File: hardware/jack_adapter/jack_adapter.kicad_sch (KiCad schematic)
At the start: 14 parts, among them J1 2.5mm Mic, J2 AudioPlug3, J3 3.5mm Headphones, J4 Header, SW1 SW_SPDT, SW2 SW_SPST

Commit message: feat: Moved the jacks slightly to be inline diagonally
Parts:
- J1: JLCPCB Part # C431535 -> C431536
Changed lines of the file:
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@@
 			)
 		)
-		(property "JLCPCB Part #" "C431535"
+		(property "JLCPCB Part #" "C431536"
 			(at 49.53 86.36 0)
 			(effects

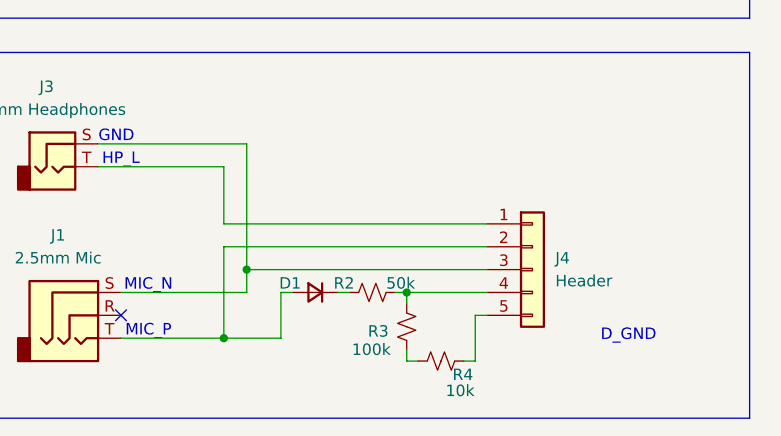
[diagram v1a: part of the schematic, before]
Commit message: feat: Changed resistor part number, and jumpers, and re-arranged things a bit
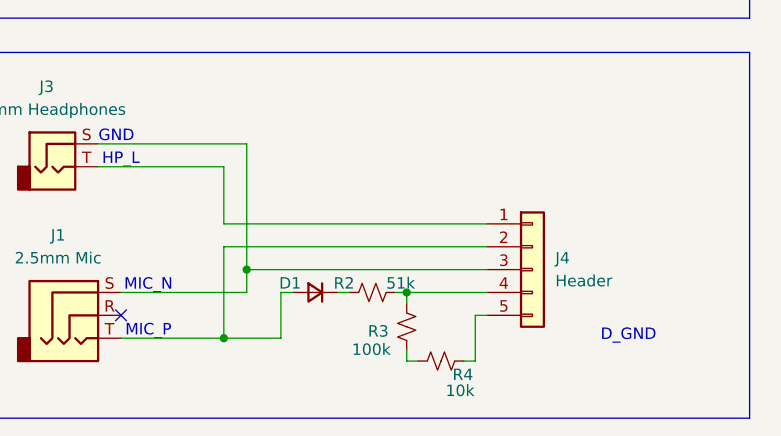
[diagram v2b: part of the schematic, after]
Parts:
- D1: FT Rotation Offset (none) -> 180
- J1: FT Rotation Offset (none) -> 90
- J3: FT Position Offset (none) -> 0.889,0; FT Rotation Offset (none) -> 90
- J4: FT Rotation Offset (none) -> 90; JLCPCB Part # C2718488 -> C5116488
- R2: value 50k -> 51k; footprint Resistor_SMD:R_0402_1005Metric -> Resistor_SMD:R_0805_2012Metric; JLCPCB Part # C25794 -> C17737
- R3: footprint Resistor_SMD:R_0402_1005Metric -> Resistor_SMD:R_0805_2012Metric; JLCPCB Part # C25741 -> C149504
- R4: footprint Resistor_SMD:R_0402_1005Metric -> Resistor_SMD:R_0805_2012Metric; JLCPCB Part # C25744 -> C17414
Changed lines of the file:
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@@
 			)
 		)
-		(property "Footprint" "Resistor_SMD:R_0402_1005Metric"
+		(property "Footprint" "Resistor_SMD:R_0805_2012Metric"
 			(at 90.17 91.44 0)
 			(effects
@@
 			)
 		)
-		(property "JLCPCB Part #" "C25744"
+		(property "JLCPCB Part #" "C17414"
 			(at 90.17 91.44 0)
 			(effects
@@
 			)
 		)
-		(property "JLCPCB Part #" "C2718488"
+		(property "JLCPCB Part #" "C5116488"
+			(at 100.33 81.28 0)
+			(effects
+				(font
+					(size 1.27 1.27)
+				)
+				(hide yes)
+			)
+		)
+		(property "FT Rotation Offset" "90"
 			(at 100.33 81.28 0)
 			(effects
@@
 			)
 		)
+		(property "FT Rotation Offset" "90"
+			(at 49.53 86.36 0)
+			(effects
+				(font
+					(size 1.27 1.27)
+				)
+				(hide yes)
+			)
+		)
 		(pin "T"
 		)
@@
 			)
 		)
+		(property "FT Rotation Offset" "180"
+			(at 76.2 83.82 0)
+			(effects
+				(font
+					(size 1.27 1.27)
+				)
+				(hide yes)
+			)
+		)
 		(pin "1"
 		)
@@
 			)
 		)
-		(property "Value" "50k"
+		(property "Value" "51k"
 			(at 84.074 82.804 90)
 			(effects
@@
 			)
 		)
-		(property "Footprint" "Resistor_SMD:R_0402_1005Metric"
+		(property "Footprint" "Resistor_SMD:R_0805_2012Metric"
 			(at 82.55 83.82 0)
 			(effects
@@
 			)
 		)
-		(property "JLCPCB Part #" "C25794"
+		(property "JLCPCB Part #" "C17737"
 			(at 82.55 83.82 0)
 			(effects
@@
 			)
 		)
-		(property "Footprint" "Resistor_SMD:R_0402_1005Metric"
+		(property "Footprint" "Resistor_SMD:R_0805_2012Metric"
 			(at 86.36 87.63 0)
 			(effects
@@
 			)
 		)
-		(property "JLCPCB Part #" "C25741"
+		(property "JLCPCB Part #" "C149504"
 			(at 86.36 87.63 0)
 			(effects
@@
 			(at 46.99 69.85 0)
 			(effects
+				(font
+					(size 1.27 1.27)
+				)
+				(hide yes)
+			)
+		)
+		(property "FT Rotation Offset" "90"
+			(at 46.99 69.85 0)
+			(effects
+				(font
+					(size 1.27 1.27)
+				)
+				(hide yes)
+			)
+		)
+		(property "FT Position Offset" "0.889,0"
+			(at 46.99 69.85 0)
+			(effects

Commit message: chore: fix misaligned 2.5mm jack
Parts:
- J3: footprint Connector_Audio:Jack_3.5mm_PJ320D_Horizontal -> hactar_lib:Jack_3.5mm_PJ320D_Horizontal; FT Position Offset 0.889,0 -> 1.016,0
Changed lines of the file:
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@@
 			)
 		)
-		(property "Footprint" "Connector_Audio:Jack_3.5mm_PJ320D_Horizontal"
+		(property "Footprint" "hactar_lib:Jack_3.5mm_PJ320D_Horizontal"
 			(at 46.99 69.85 0)
 			(effects
@@
 			)
 		)
-		(property "FT Position Offset" "0.889,0"
+		(property "FT Position Offset" "1.016,0"
 			(at 46.99 69.85 0)
 			(effects

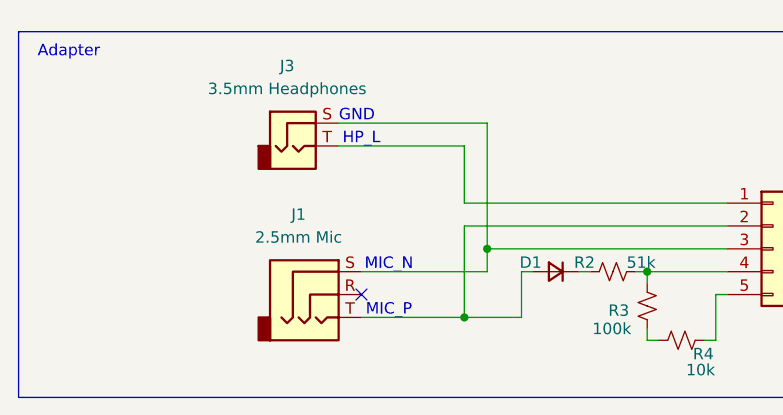
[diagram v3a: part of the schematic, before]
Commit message: bugfix: updated the footprint to be what it actually is a TRRS and match what the datasheet says. As well, updated the sch to match that it is a TRRS
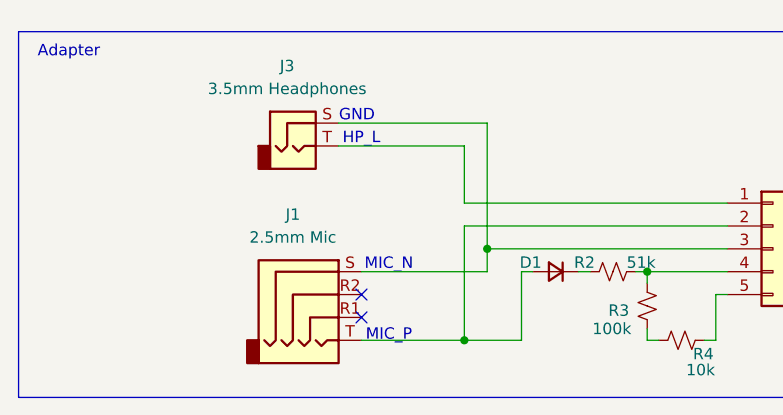
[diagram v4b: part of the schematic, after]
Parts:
- J1: symbol Connector_Audio:AudioJack3 -> Connector_Audio:AudioJack4
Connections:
- no-connect marks 2 -> 3
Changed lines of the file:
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@@
 	(text "MIC_P"
 		(exclude_from_sim no)
-		(at 57.658 88.138 0)
+		(at 57.658 90.932 0)
 		(effects
 			(font
@@
 	)
 	(junction
+		(at 66.04 91.44)
+		(diameter 0)
+		(color 0 0 0 0)
+	)
+	(junction
 		(at 30.48 46.99)
 		(diameter 0)
@@
 		(color 0 0 0 0)
 	)
-	(junction
-		(at 66.04 88.9)
-		(diameter 0)
-		(color 0 0 0 0)
-	)
 	(no_connect
 		(at 54.61 86.36)
@@
 		(at 83.82 40.64)
 	)
+	(no_connect
+		(at 54.61 88.9)
+	)
 	(wire
 		(pts
@@
 	(wire
 		(pts
+			(xy 66.04 91.44) (xy 54.61 91.44)
+		)
+		(stroke
+			(width 0)
+			(type default)
+		)
+	)
+	(wire
+		(pts
 			(xy 73.66 34.29) (xy 63.5 34.29)
 		)
@@
 	(wire
 		(pts
-			(xy 72.39 88.9) (xy 66.04 88.9)
+			(xy 72.39 91.44) (xy 66.04 91.44)
 		)
 		(stroke
@@
 	(wire
 		(pts
+			(xy 66.04 78.74) (xy 66.04 91.44)
+		)
+		(stroke
+			(width 0)
+			(type default)
+		)
+	)
+	(wire
+		(pts
 			(xy 54.61 83.82) (xy 68.58 83.82)
 		)
@@
 	(wire
 		(pts
-			(xy 66.04 78.74) (xy 66.04 88.9)
-		)
-		(stroke
-			(width 0)
-			(type default)
-		)
-	)
-	(wire
-		(pts
 			(xy 73.66 46.99) (xy 81.28 46.99)
 		)
@@
 	(wire
 		(pts
-			(xy 54.61 88.9) (xy 66.04 88.9)
-		)
-		(stroke
-			(width 0)
-			(type default)
-		)
-	)
-	(wire
-		(pts
 			(xy 50.8 34.29) (xy 46.99 34.29)
 		)
@@
 	(wire
 		(pts
-			(xy 72.39 83.82) (xy 72.39 88.9)
+			(xy 72.39 83.82) (xy 72.39 91.44)
 		)
 		(stroke
@@
 	)
 	(symbol
-		(lib_id "Connector_Audio:AudioJack3")
+		(lib_id "Connector_Audio:AudioJack4")
 		(at 49.53 86.36 0)
 		(unit 1)
@@
 		(fields_autoplaced yes)
 		(property "Reference" "J1"
-			(at 47.625 77.47 0)
+			(at 46.99 77.47 0)
 			(effects
 				(font
@@
 		)
 		(property "Value" "2.5mm Mic"
-			(at 47.625 80.01 0)
+			(at 46.99 80.01 0)
 			(effects
 				(font
@@
 			)
 		)
-		(property "Description" "Audio Jack, 3 Poles (Stereo / TRS)"
+		(property "Description" "Audio Jack, 4 Poles (TRRS)"
 			(at 49.53 86.36 0)
 			(effects
@@
 		(pin "S"
 		)
-		(pin "R"
+		(pin "R1"
+		)
+		(pin "R2"
 		)
 		(instances

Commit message: bugfix: cleanup the schematic and pcb
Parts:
- J3: symbol Connector_Audio:AudioJack2 -> Connector_Audio:AudioJack4
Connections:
- no-connect marks 3 -> 5
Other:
- moved on the sheet: J1
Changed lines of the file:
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@@
 	(rectangle
 		(start 16.51 57.15)
-		(end 124.46 97.79)
+		(end 124.46 106.68)
 		(stroke
 			(width 0)
@@
 	(text "HP_L"
 		(exclude_from_sim no)
-		(at 54.61 69.088 0)
+		(at 58.166 75.438 0)
 		(effects
 			(font
@@
 	(text "MIC_P"
 		(exclude_from_sim no)
-		(at 57.658 90.932 0)
+		(at 58.674 93.218 0)
 		(effects
 			(font
@@
 	(text "MIC_N"
 		(exclude_from_sim no)
-		(at 57.658 83.058 0)
+		(at 58.674 85.598 0)
 		(effects
 			(font
@@
 	(text "GND"
 		(exclude_from_sim no)
-		(at 54.102 66.548 0)
+		(at 57.912 67.818 0)
 		(effects
 			(font
@@
 	)
 	(no_connect
-		(at 54.61 86.36)
+		(at 54.61 88.9)
 	)
 	(no_connect
@@
 	)
 	(no_connect
-		(at 54.61 88.9)
+		(at 54.61 73.66)
+	)
+	(no_connect
+		(at 54.61 91.44)
+	)
+	(no_connect
+		(at 54.61 71.12)
 	)
 	(wire
@@
 	(wire
 		(pts
-			(xy 68.58 81.28) (xy 68.58 83.82)
+			(xy 68.58 81.28) (xy 68.58 86.36)
 		)
 		(stroke
@@
 	(wire
 		(pts
-			(xy 66.04 91.44) (xy 54.61 91.44)
+			(xy 66.04 93.98) (xy 54.61 93.98)
 		)
 		(stroke
@@
 	(wire
 		(pts
-			(xy 66.04 76.2) (xy 95.25 76.2)
-		)
-		(stroke
-			(width 0)
-			(type default)
-		)
-	)
-	(wire
-		(pts
-			(xy 68.58 67.31) (xy 68.58 81.28)
+			(xy 68.58 68.58) (xy 68.58 81.28)
 		)
 		(stroke
@@
 	(wire
 		(pts
-			(xy 52.07 67.31) (xy 68.58 67.31)
+			(xy 54.61 68.58) (xy 68.58 68.58)
 		)
 		(stroke
@@
 	(wire
 		(pts
-			(xy 54.61 83.82) (xy 68.58 83.82)
+			(xy 54.61 86.36) (xy 68.58 86.36)
 		)
 		(stroke
@@
 	(wire
 		(pts
-			(xy 52.07 69.85) (xy 66.04 69.85)
+			(xy 66.04 93.98) (xy 66.04 91.44)
 		)
 		(stroke
@@
 	(wire
 		(pts
-			(xy 66.04 69.85) (xy 66.04 76.2)
-		)
-		(stroke
-			(width 0)
-			(type default)
-		)
-	)
-	(wire
-		(pts
 			(xy 63.5 34.29) (xy 63.5 38.1)
 		)
@@
 		(pts
 			(xy 86.36 91.44) (xy 86.36 90.17)
+		)
+		(stroke
+			(width 0)
+			(type default)
+		)
+	)
+	(wire
+		(pts
+			(xy 54.61 76.2) (xy 95.25 76.2)
 		)
 		(stroke
@@
 	(symbol
 		(lib_id "Connector_Audio:AudioJack4")
-		(at 49.53 86.36 0)
+		(at 49.53 88.9 0)
 		(unit 1)
 		(exclude_from_sim no)
@@
 		(fields_autoplaced yes)
 		(property "Reference" "J1"
-			(at 46.99 77.47 0)
+			(at 46.99 80.01 0)
 			(effects
 				(font
@@
 		)
 		(property "Value" "2.5mm Mic"
-			(at 46.99 80.01 0)
+			(at 46.99 82.55 0)
 			(effects
 				(font
@@
 		)
 		(property "Footprint" "hactar_lib:AUDIO-SMD_PJ-242D-SMT"
-			(at 49.53 86.36 0)
+			(at 49.53 88.9 0)
 			(effects
 				(font
@@
 		)
 		(property "Datasheet" "~"
-			(at 49.53 86.36 0)
+			(at 49.53 88.9 0)
 			(effects
 				(font
@@
 		)
 		(property "Description" "Audio Jack, 4 Poles (TRRS)"
-			(at 49.53 86.36 0)
+			(at 49.53 88.9 0)
 			(effects
 				(font
@@
 		)
 		(property "JLCPCB Part #" "C431536"
-			(at 49.53 86.36 0)
+			(at 49.53 88.9 0)
 			(effects
 				(font
@@
 		)
 		(property "FT Rotation Offset" "90"
-			(at 49.53 86.36 0)
+			(at 49.53 88.9 0)
 			(effects
 				(font
@@
 	)
 	(symbol
-		(lib_id "Connector_Audio:AudioJack2")
-		(at 46.99 69.85 0)
+		(lib_id "Connector_Audio:AudioJack4")
+		(at 49.53 71.12 0)
 		(unit 1)
 		(exclude_from_sim no)
@@
 		(fields_autoplaced yes)
 		(property "Reference" "J3"
-			(at 46.355 60.96 0)
+			(at 46.99 62.23 0)
 			(effects
 				(font
@@
 		)
 		(property "Value" "3.5mm Headphones"
-			(at 46.355 63.5 0)
+			(at 46.99 64.77 0)
 			(effects
 				(font
@@
 		)
 		(property "Footprint" "hactar_lib:Jack_3.5mm_PJ320D_Horizontal"
-			(at 46.99 69.85 0)
+			(at 49.53 71.12 0)
 			(effects
 				(font
@@
 		)
 		(property "Datasheet" "~"
-			(at 46.99 69.85 0)
-			(effects
-				(font
-					(size 1.27 1.27)
-				)
-				(hide yes)
-			)
-		)
-		(property "Description" "Audio Jack, 2 Poles (Mono / TS)"
-			(at 46.99 69.85 0)
+			(at 49.53 71.12 0)
+			(effects
+				(font
+					(size 1.27 1.27)
+				)
+				(hide yes)
+			)
+		)
+		(property "Description" "Audio Jack, 4 Poles (TRRS)"
+			(at 49.53 71.12 0)
 			(effects
 				(font
@@
 		)
 		(property "JLCPCB Part #" "C431535"
-			(at 46.99 69.85 0)
+			(at 49.53 71.12 0)
 			(effects
 				(font
@@
 		)
 		(property "FT Rotation Offset" "90"
-			(at 46.99 69.85 0)
+			(at 49.53 71.12 0)
 			(effects
 				(font
@@
 		)
 		(property "FT Position Offset" "1.016,0"
-			(at 46.99 69.85 0)
+			(at 49.53 71.12 0)
 			(effects
 				(font
@@
 		(pin "T"
 		)
+		(pin "R2"
+		)
+		(pin "R1"
+		)
 		(instances
